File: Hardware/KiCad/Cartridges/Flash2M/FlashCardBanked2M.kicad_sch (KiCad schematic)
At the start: 9 parts, among them IC1 AS29CF160B-55TIN, IC2 74595D, IC3 74244DW, IC4 74HC1G04GW

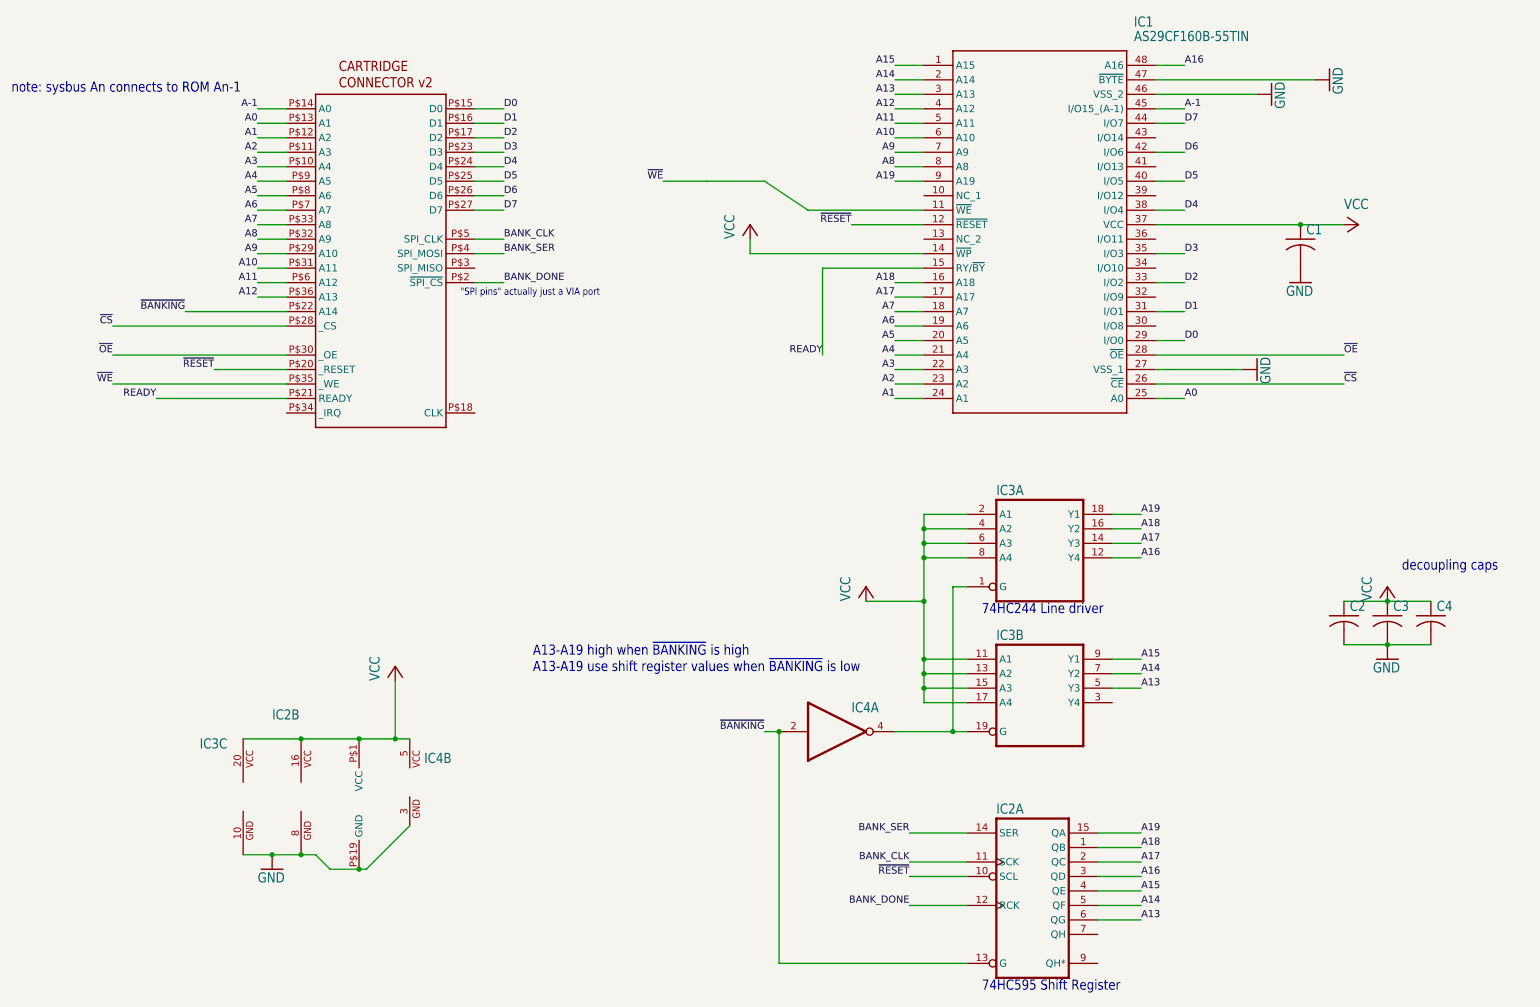
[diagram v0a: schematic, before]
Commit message: add footprint for reset controller on logic board and remove READY on cartridges
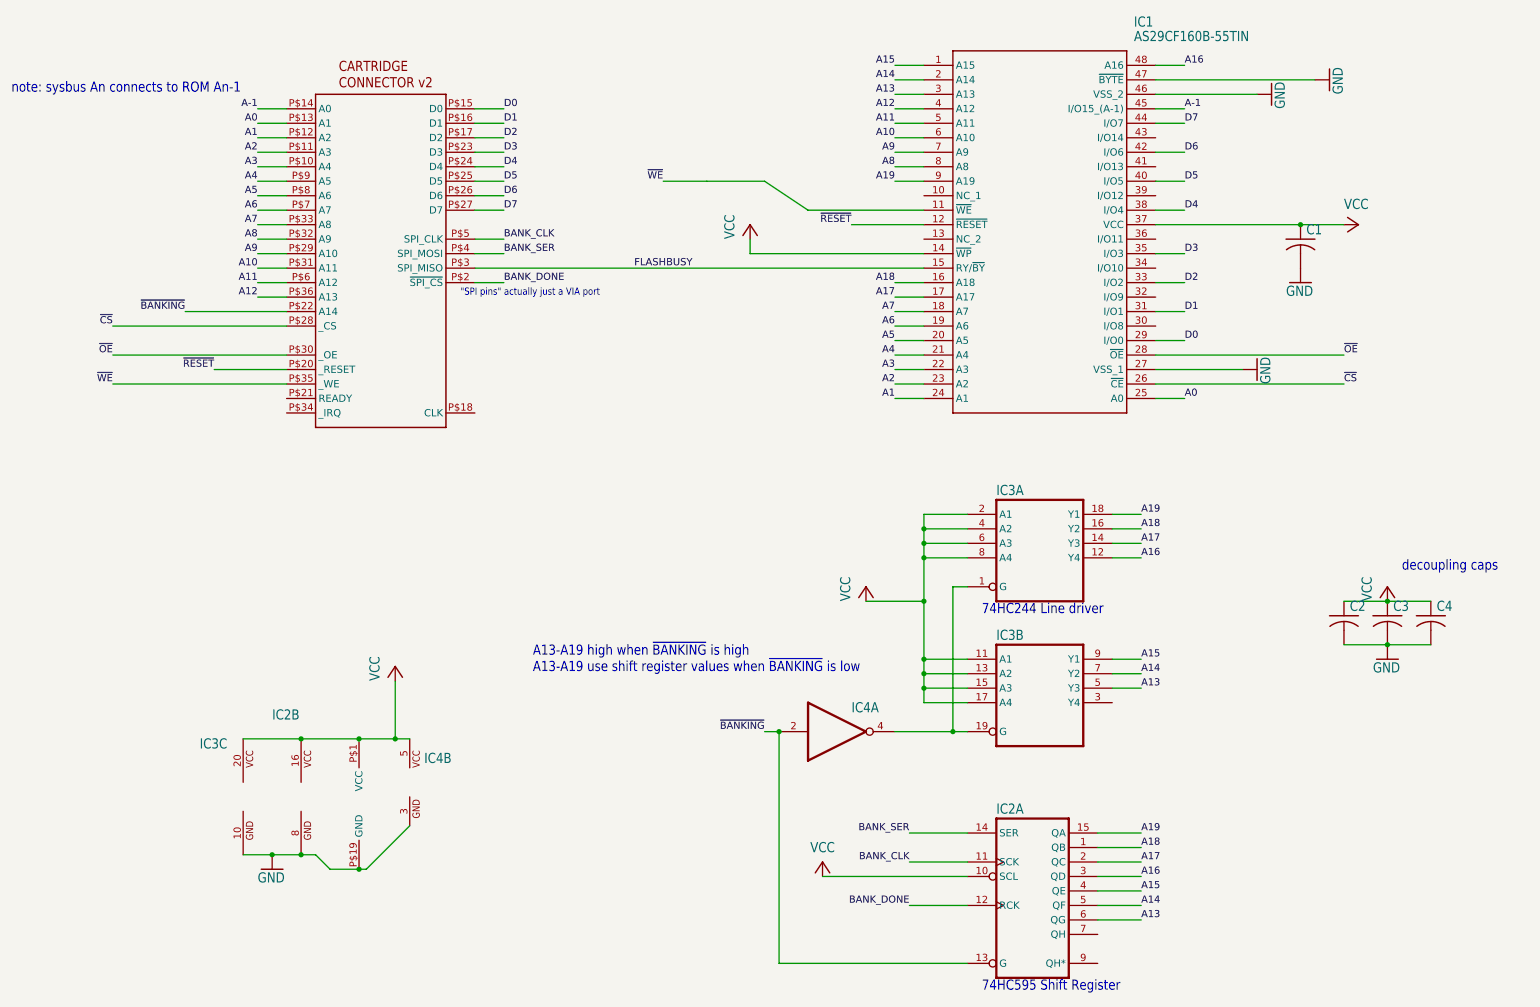
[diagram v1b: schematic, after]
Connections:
- net VCC: now also IC2.10 (SCL)
- net ~{RESET}: no longer IC2.10 (SCL)
- net FLASHBUSY: now reaches U$1.P$3 (SPI_MISO)
- net FLASHBUSY: now also IC1.15 (RY/~{BY})
- net READY: no longer names the net of U$1.P$21 (READY)
- net READY: no longer IC1.15 (RY/~{BY})
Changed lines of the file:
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@@
-    (stroke (width 0.1524) (type solid))
-  )
-  (wire (pts (xy 185.42 170.18) (xy 175.26 170.18))
     (stroke (width 0.1524) (type solid))
   )
@@
     (stroke (width 0.1524) (type solid))
   )
+  (wire (pts (xy 160.02 170.18) (xy 185.42 170.18))
+    (stroke (width 0) (type default))
+  )
   (wire (pts (xy 177.8 55.88) (xy 165.1 55.88))
     (stroke (width 0.1524) (type solid))
@@
     (stroke (width 0.1524) (type solid))
   )
-  (wire (pts (xy 177.8 63.5) (xy 160.02 63.5))
-    (stroke (width 0.1524) (type solid))
-  )
   (wire (pts (xy 99.06 50.8) (xy 104.14 50.8))
     (stroke (width 0.1524) (type solid))
@@
     (stroke (width 0.1524) (type solid))
   )
+  (wire (pts (xy 99.06 63.5) (xy 177.8 63.5))
+    (stroke (width 0) (type default))
+  )
   (wire (pts (xy 177.8 83.82) (xy 172.72 83.82))
     (stroke (width 0.1524) (type solid))
@@
     (stroke (width 0.1524) (type solid))
   )
-  (wire (pts (xy 160.02 63.5) (xy 160.02 78.74))
-    (stroke (width 0.1524) (type solid))
-  )
   (wire (pts (xy 58.42 146.05) (xy 68.58 146.05))
     (stroke (width 0) (type default))
@@
   )
   (wire (pts (xy 208.28 172.72) (xy 215.9 172.72))
-    (stroke (width 0.1524) (type solid))
-  )
-  (wire (pts (xy 66.04 86.36) (xy 43.18 86.36))
     (stroke (width 0.1524) (type solid))
   )
@@
     (effects (font (size 1.2446 1.2446)) (justify right bottom))
   )
-  (label "~{RESET}" (at 175.26 170.18 180) (fields_autoplaced)
-    (effects (font (size 1.2446 1.2446)) (justify right bottom))
-  )
   (label "~{OE}" (at 35.56 78.74 180) (fields_autoplaced)
     (effects (font (size 1.2446 1.2446)) (justify right bottom))
@@
     (effects (font (size 1.2446 1.2446)) (justify left bottom))
   )
-  (label "READY" (at 43.18 86.36 180) (fields_autoplaced)
-    (effects (font (size 1.2446 1.2446)) (justify right bottom))
-  )
   (label "A19" (at 215.9 106.68 0) (fields_autoplaced)
     (effects (font (size 1.2446 1.2446)) (justify left bottom))
@@
     (effects (font (size 1.2446 1.2446)) (justify right bottom))
   )
+  (label "FLASHBUSY" (at 127 63.5 0) (fields_autoplaced)
+    (effects (font (size 1.27 1.27)) (justify left bottom))
+  )
   (label "A12" (at 172.72 35.56 180) (fields_autoplaced)
-    (effects (font (size 1.2446 1.2446)) (justify right bottom))
-  )
-  (label "READY" (at 160.02 78.74 180) (fields_autoplaced)
     (effects (font (size 1.2446 1.2446)) (justify right bottom))
   )
@@
         )
       )
+    )
+  )
+  (symbol (lib_id "FlashCardBanked2M-eagle-import:VCC") (at 160.02 167.64 0) (unit 1)
+    (in_bom yes) (on_board yes) (dnp no) (fields_autoplaced)
+    (property "Reference" "#P+06" (at 160.02 167.64 0)
+      (effects (font (size 1.27 1.27)) hide)
+    )
+    (property "Value" "VCC" (at 160.02 165.1 0)
+      (effects (font (size 1.778 1.5113)))
+    )
+    (property "Footprint" "" (at 160.02 167.64 0)
+      (effects (font (size 1.27 1.27)) hide)
+    )
+    (property "Datasheet" "" (at 160.02 167.64 0)
+      (effects (font (size 1.27 1.27)) hide)
+    )
+    (pin "1")
+    (instances
+      (project "FlashCardBanked2M"
+        (path "/efb4bb42-9307-46c9-89da-d677369b1356"
+          (reference "#P+06") (unit 1)
+        )
+      )

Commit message: updates
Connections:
- net A13: now also IC2.15 (QA); no longer IC2.6 (QG)
- net A14: now also IC2.1 (QB); no longer IC2.5 (QF)
- net A15: now also IC2.2 (QC); no longer IC2.4 (QE)
- net A17: now also IC2.4 (QE); no longer IC2.2 (QC)
- net A18: now also IC2.5 (QF); no longer IC2.1 (QB)
- net A19: now also IC2.6 (QG); no longer IC2.15 (QA)
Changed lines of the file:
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@@
+	(wire
+		(pts
+			(xy 217.17 170.18) (xy 208.28 170.18)
+		)
+		(stroke
+			(width 0)
+			(type default)
+		)
+	)
+	(wire
+		(pts
+			(xy 217.17 165.1) (xy 208.28 165.1)
+		)
+		(stroke
+			(width 0)
+			(type default)
+		)
+	)
 	(wire
 		(pts
@@
 	(wire
 		(pts
-			(xy 208.28 165.1) (xy 215.9 165.1)
-		)
-		(stroke
-			(width 0.1524)
-			(type solid)
-		)
-	)
-	(wire
-		(pts
 			(xy 66.04 53.34) (xy 60.96 53.34)
 		)
@@
 	(wire
 		(pts
+			(xy 217.17 172.72) (xy 208.28 172.72)
+		)
+		(stroke
+			(width 0)
+			(type default)
+		)
+	)
+	(wire
+		(pts
 			(xy 99.06 50.8) (xy 104.14 50.8)
 		)
@@
 	(wire
 		(pts
-			(xy 208.28 167.64) (xy 215.9 167.64)
-		)
-		(stroke
-			(width 0.1524)
-			(type solid)
-		)
-	)
-	(wire
-		(pts
 			(xy 177.8 114.3) (xy 177.8 121.92)
 		)
@@
 	(wire
 		(pts
-			(xy 208.28 177.8) (xy 215.9 177.8)
-		)
-		(stroke
-			(width 0.1524)
-			(type solid)
-		)
-	)
-	(wire
-		(pts
 			(xy 66.04 35.56) (xy 60.96 35.56)
 		)
@@
 	(wire
 		(pts
+			(xy 217.17 175.26) (xy 208.28 175.26)
+		)
+		(stroke
+			(width 0)
+			(type default)
+		)
+	)
+	(wire
+		(pts
 			(xy 185.42 137.16) (xy 177.8 137.16)
 		)
@@
 	(wire
 		(pts
-			(xy 208.28 170.18) (xy 215.9 170.18)
-		)
-		(stroke
-			(width 0.1524)
-			(type solid)
-		)
-	)
-	(wire
-		(pts
 			(xy 139.7 48.26) (xy 149.86 48.26)
 		)
@@
 	(wire
 		(pts
+			(xy 217.17 162.56) (xy 208.28 162.56)
+		)
+		(stroke
+			(width 0)
+			(type default)
+		)
+	)
+	(wire
+		(pts
 			(xy 66.04 55.88) (xy 60.96 55.88)
 		)
@@
 	(wire
 		(pts
-			(xy 208.28 172.72) (xy 215.9 172.72)
-		)
-		(stroke
-			(width 0.1524)
-			(type solid)
-		)
-	)
-	(wire
-		(pts
 			(xy 185.42 106.68) (xy 177.8 106.68)
 		)
@@
 	(wire
 		(pts
-			(xy 208.28 175.26) (xy 215.9 175.26)
-		)
-		(stroke
-			(width 0.1524)
-			(type solid)
-		)
-	)
-	(wire
-		(pts
-			(xy 208.28 162.56) (xy 215.9 162.56)
-		)
-		(stroke
-			(width 0.1524)
-			(type solid)
+			(xy 217.17 167.64) (xy 208.28 167.64)
+		)
+		(stroke
+			(width 0)
+			(type default)
+		)
+	)
+	(wire
+		(pts
+			(xy 217.17 177.8) (xy 208.28 177.8)
+		)
+		(stroke
+			(width 0)
+			(type default)
 		)
 	)
@@
 	)
 	(label "A16"
-		(at 215.9 170.18 0)
+		(at 217.17 170.18 0)
 		(effects
 			(font
@@
 	)
 	(label "A18"
-		(at 215.9 165.1 0)
+		(at 217.17 175.26 0)
 		(effects
 			(font
@@
 	)
 	(label "A14"
-		(at 215.9 175.26 0)
+		(at 217.17 165.1 0)
 		(effects
 			(font
@@
 	)
 	(label "A15"
-		(at 215.9 172.72 0)
+		(at 217.17 167.64 0)
 		(effects
 			(font
@@
 	)
 	(label "A17"
-		(at 215.9 167.64 0)
+		(at 217.17 172.72 0)
 		(effects
 			(font
@@
 	)
 	(label "A13"
-		(at 215.9 177.8 0)
+		(at 217.17 162.56 0)
 		(effects
 			(font
@@
 	)
 	(label "A19"
-		(at 215.9 162.56 0)
-		(effects
-			(font
+		(at 217.17 177.8 0)
+		(effects
+			(font
